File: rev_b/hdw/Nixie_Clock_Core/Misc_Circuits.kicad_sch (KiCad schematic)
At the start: 20 parts, among them U2401 LTC6900, U2402 74LVC1G08

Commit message: lots of rev B control board schematic progress
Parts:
- removed D?: MBR0580, Diode_SMD:D_SOD-123, symbol Diode:MBR0580
- removed U2402: 74LVC1G08, Package_TO_SOT_SMD:SOT-353_SC-70-5, symbol Custom_Library:74LVC1G08_Power
- added D?: SMD1200PL, Diodes_SMD:D_SOD-123F, symbol Nixie-Clock-rescue:D_Schottky
- added U?: 74LVC1G97, Package_TO_SOT_SMD:SOT-363_SC-70-6, symbol Custom Library:74LVC1G97_Power_AND
- renumbered BZ2401 to BZ?, R2406 to R?, U2401 to U?
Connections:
- net +3.3V: now also D?.1 (K), U?.5 (VCC)
- net Buzzer_Enable: now also U?.3
- net GND: now also U?.1 (GND), U?.2 (GND)
- net at BZ?.2 (+), Q?.3 (D): now also D?.2 (A)
- net at R?.2, U?.5 (OUT): now also U?.6
- net at R?.2: now also U?.4

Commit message: more rev b sch progress
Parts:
- removed J?: DAC SPI, Pin_Headers:Pin_Header_Straight_1x03_Pitch2.54mm, symbol Connector_Generic:Conn_01x03
- added R? (x2): 10k, Resistors_SMD:R_0603, symbol Custom_Library:R_Custom
- added R? (x2): 10, Resistors_SMD:R_0603, symbol Custom_Library:R_Custom
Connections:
- net +3.3V: now also R?.1, R?.1
- net GND: now also R?.2, R?.2
- new net ETC_Hardstrap: R?.1, R?.2
- new net RTC_Hardstrap: R?.1, R?.2
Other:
- moved on the sheet: BZ?, C?, D?, J?, Q?, R?, U?

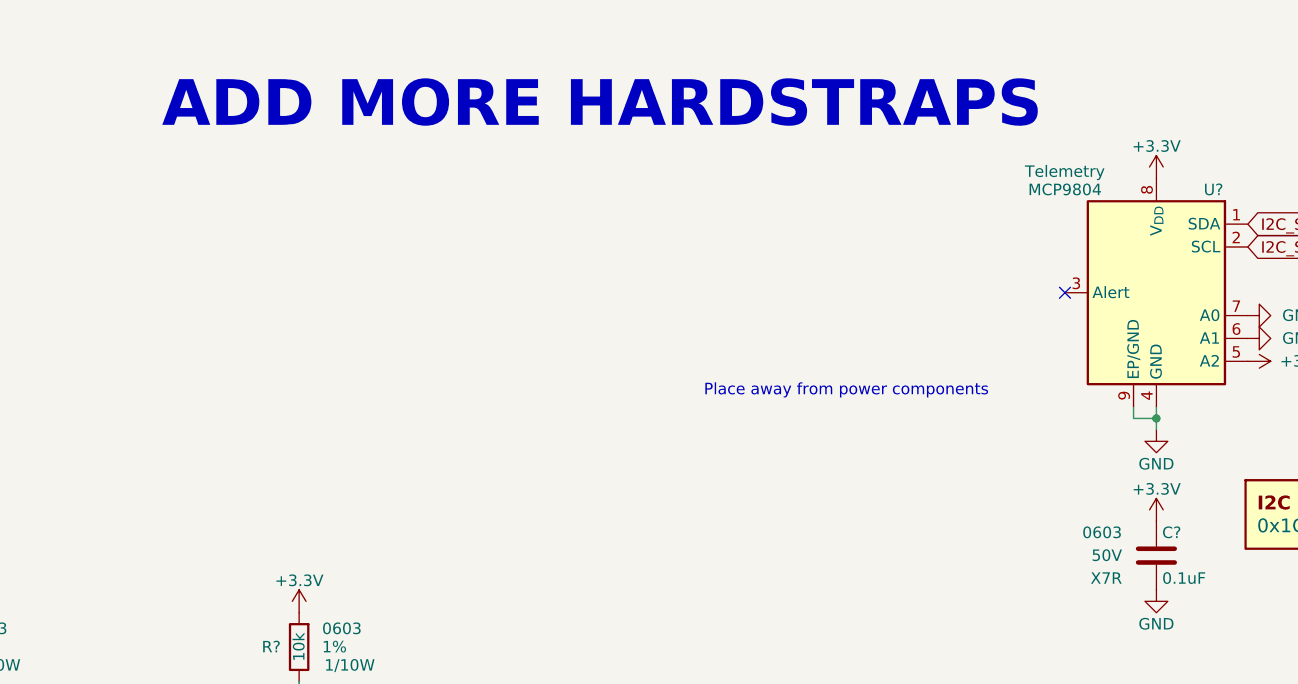
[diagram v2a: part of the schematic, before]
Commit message: more schematic progress, assigning signals to MCU"
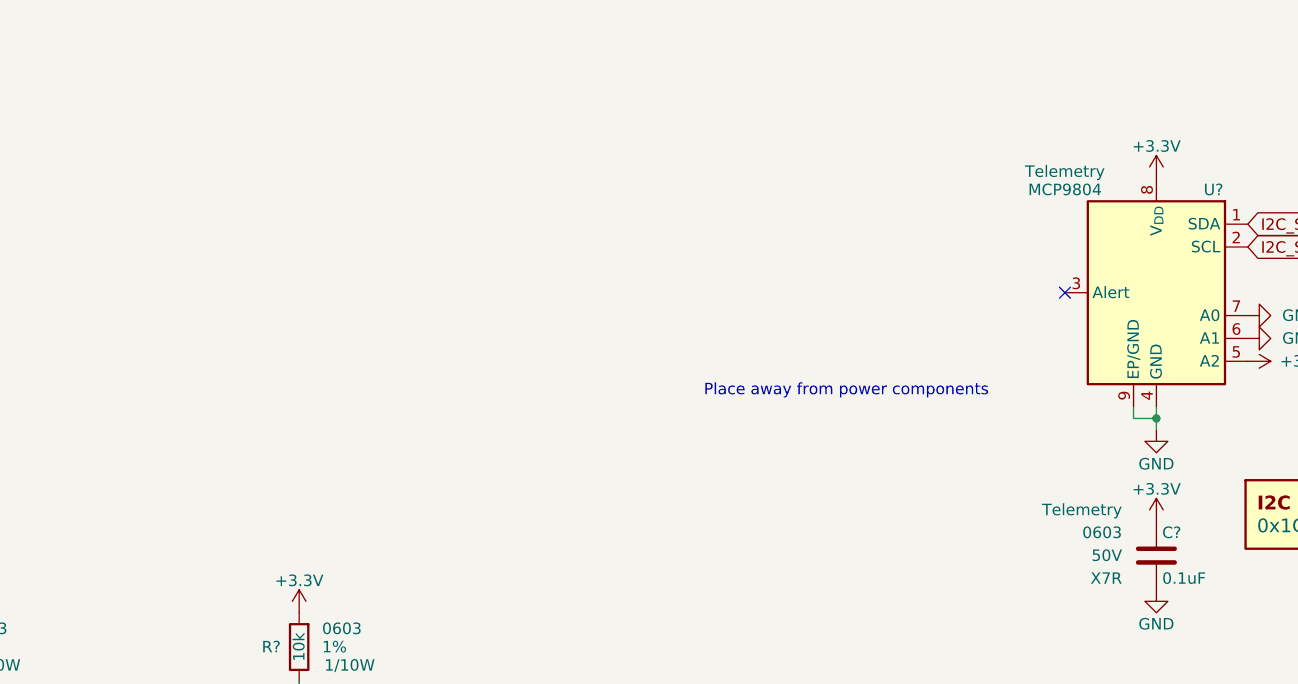
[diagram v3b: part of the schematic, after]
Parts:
- C?: Configuration (none) -> Telemetry
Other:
- note removed: "ADD MORE HARDSTRAPS"
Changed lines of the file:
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@@
     (stroke (width 0) (type default))
-  )
-  (text "ADD MORE HARDSTRAPS" (at 96.52 31.75 0)
-    (effects (font (face "Courier New") (size 5.08 5.08) (thickness 0.254) bold (color 255 37 56 1)) (justify left bottom))
   )
   (text "Fosc ~ 2kHz" (at 53.213 158.115 0)
@@
       (effects (font (size 1.27 1.27)) hide)
     )
-    (pin "1")
+    (property "Configuration" "Telemetry" (at 203.2 73.66 0)
+      (effects (font (size 1.27 1.27)) (justify right))
+    )
+    (pin "1")

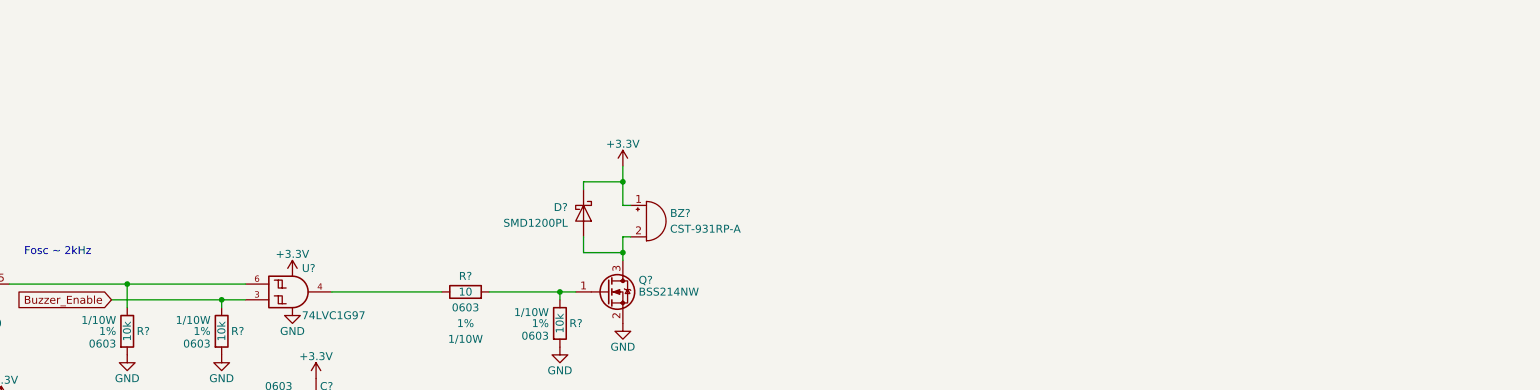
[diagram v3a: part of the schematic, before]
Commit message: updated footprints, ran some DRC
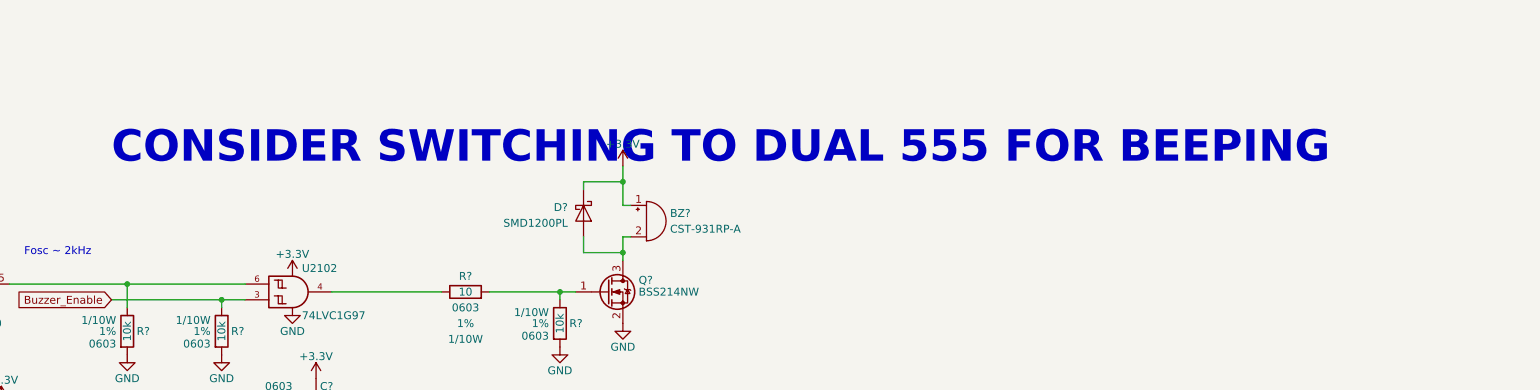
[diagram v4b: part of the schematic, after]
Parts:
- C? (x3): Digi-Key PN 399-7845-1-ND -> (none)
- D?: Footprint Display SOD-123F -> (none); display_footprint (none) -> SOD-123F
- J? (x2): footprint Pin_Headers:Pin_Header_Straight_1x03_Pitch2.54mm -> Connector_PinHeader_2.54mm:PinHeader_1x03_P2.54mm_Vertical
- Q?: footprint TO_SOT_Packages_SMD:SOT-323_SC-70 -> Package_TO_SOT_SMD:SOT-323_SC-70
- R? (x7): Digi-Key PN YAG2321CT-ND -> (none)
- R?: Digi-Key PN RMCF0603FT1M07CT-ND -> (none)
- gave numbers to parts that had none: 1
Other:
- note added: "CONSIDER SWITCHING TO DUAL 555 FOR BEEPING"

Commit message: hid all passive refdes on core PCB
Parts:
- C? (x3): Digi-Key PN (none) -> 1276-1935-1-ND
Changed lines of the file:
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@@
       (effects (font (size 1.27 1.27)) (justify right))
     )
-    (property "Digi-Key PN" "" (at 1.016 356.362 0)
+    (property "Digi-Key PN" "1276-1935-1-ND" (at 1.016 356.362 0)
       (effects (font (size 1.27 1.27)) hide)
     )
@@
       (effects (font (size 1.27 1.27)) (justify right))
     )
-    (property "Digi-Key PN" "" (at 107.696 253.492 0)
+    (property "Digi-Key PN" "1276-1935-1-ND" (at 107.696 253.492 0)
       (effects (font (size 1.27 1.27)) hide)
     )
@@
       (effects (font (size 1.27 1.27)) (justify right))
     )
-    (property "Digi-Key PN" "" (at -49.784 360.172 0)
+    (property "Digi-Key PN" "1276-1935-1-ND" (at -49.784 360.172 0)
       (effects (font (size 1.27 1.27)) hide)
     )

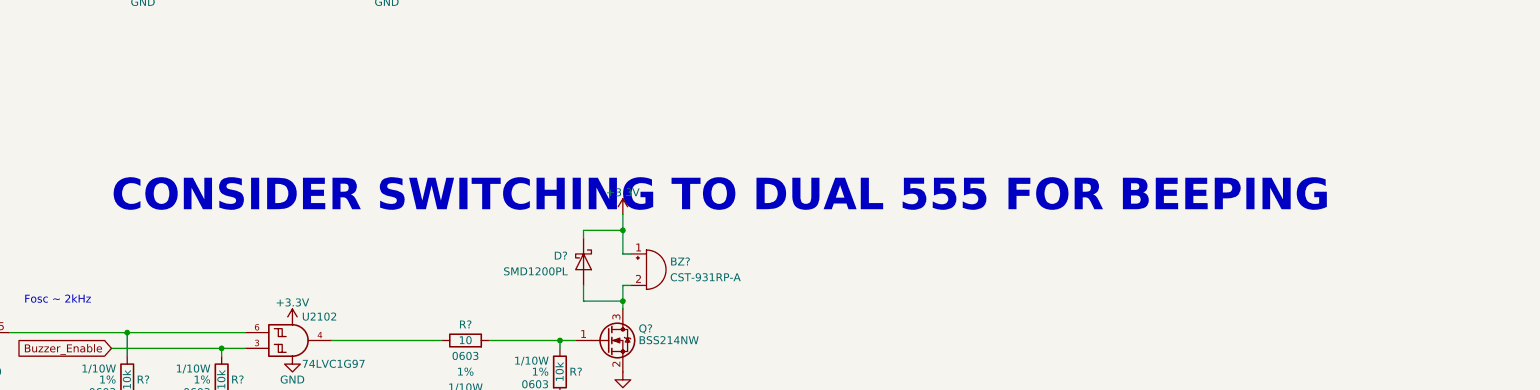
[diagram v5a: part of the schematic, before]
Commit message: added BOM
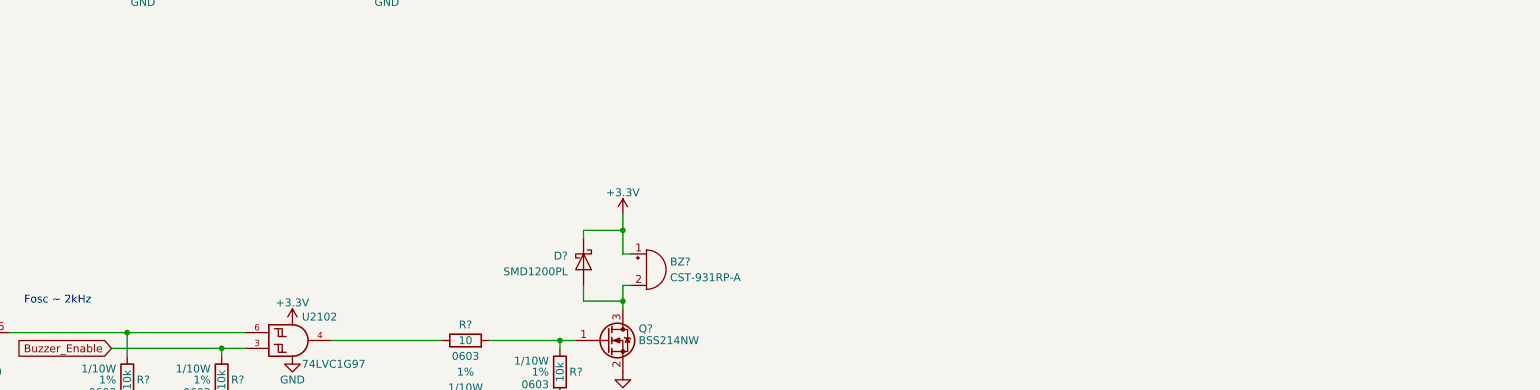
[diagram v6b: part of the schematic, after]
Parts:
- D?: Digi-Key PN (none) -> SMD1200PL-TPMSCT-ND
- R? (x4): Digi-Key PN (none) -> 541-10.0HCT-ND
- R? (x6): Digi-Key PN (none) -> 541-10.0KHCT-ND
- R?: Digi-Key PN (none) -> 541-1.07MHCT-ND
- U2102: Digi-Key PN (none) -> 296-15582-1-ND
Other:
- note removed: "CONSIDER SWITCHING TO DUAL 555 FOR BEEPING"
- company: (none) -> Drew Maatman
- title: (none) -> Nixie Clock Redux Core Board
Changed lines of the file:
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@@
 (kicad_sch (version 20230121) (generator eeschema)
   (paper "A4")
+  (title_block
+    (title "Nixie Clock Redux Core Board")
+    (date "2023-07-30")
+    (rev "B")
+    (company "Drew Maatman")
+  )
   (junction (at 111.76 95.25) (diameter 0) (color 0 0 0 0)
   )
@@
     (effects (font (size 1.27 1.27)) (justify left bottom))
   )
-  (text "CONSIDER SWITCHING TO DUAL 555 FOR BEEPING" (at 67.31 143.51 0)
-    (effects (font (face "Courier New") (size 5.08 5.08) (thickness 0.254) bold (color 255 37 56 1)) (justify left bottom))
-  )
-  (global_label "USB_UART_RX" (shape passive) (at 36.83 44.45 180)
+  (global_label "USB_UART_RX" (shape passive) (at 36.83 44.45 180) (fields_autoplaced)
     (effects (font (size 1.27 1.27)) (justify right))
-    (property "Intersheetrefs" "${INTERSHEET_REFS}" (at 36.83 44.45 0)
-      (effects (font (size 1.27 1.27)) hide)
-    )
-  )
-  (global_label "USB_UART_TX" (shape passive) (at 36.83 41.91 180)
+    (property "Intersheetrefs" "${INTERSHEET_REFS}" (at 22.1541 44.45 0)
+      (effects (font (size 1.27 1.27)) (justify right))
+    )
+  )
+  (global_label "USB_UART_TX" (shape passive) (at 36.83 41.91 180) (fields_autoplaced)
     (effects (font (size 1.27 1.27)) (justify right))
-    (property "Intersheetrefs" "${INTERSHEET_REFS}" (at 36.83 41.91 0)
-      (effects (font (size 1.27 1.27)) hide)
-    )
-  )
-  (global_label "ETC_Hardstrap" (shape passive) (at 74.93 95.25 0)
+    (property "Intersheetrefs" "${INTERSHEET_REFS}" (at 22.4565 41.91 0)
+      (effects (font (size 1.27 1.27)) (justify right))
+    )
+  )
+  (global_label "ETC_Hardstrap" (shape passive) (at 74.93 95.25 0) (fields_autoplaced)
     (effects (font (size 1.27 1.27)) (justify left))
-    (property "Intersheetrefs" "${INTERSHEET_REFS}" (at 74.93 95.25 0)
-      (effects (font (size 1.27 1.27)) hide)
-    )
-  )
-  (global_label "I2C_SDA" (shape bidirectional) (at 217.17 41.91 0)
+    (property "Intersheetrefs" "${INTERSHEET_REFS}" (at 90.3314 95.25 0)
+      (effects (font (size 1.27 1.27)) (justify left))
+    )
+  )
+  (global_label "I2C_SDA" (shape bidirectional) (at 217.17 41.91 0) (fields_autoplaced)
     (effects (font (size 1.27 1.27)) (justify left))
-    (property "Intersheetrefs" "${INTERSHEET_REFS}" (at 217.17 41.91 0)
-      (effects (font (size 1.27 1.27)) hide)
-    )
-  )
-  (global_label "RTC_Hardstrap" (shape passive) (at 114.3 95.25 0)
+    (property "Intersheetrefs" "${INTERSHEET_REFS}" (at 228.8071 41.91 0)
+      (effects (font (size 1.27 1.27)) (justify left))
+    )
+  )
+  (global_label "RTC_Hardstrap" (shape passive) (at 114.3 95.25 0) (fields_autoplaced)
     (effects (font (size 1.27 1.27)) (justify left))
-    (property "Intersheetrefs" "${INTERSHEET_REFS}" (at 114.3 95.25 0)
-      (effects (font (size 1.27 1.27)) hide)
-    )
-  )
-  (global_label "Buzzer_Enable" (shape input) (at 67.31 165.1 180)
+    (property "Intersheetrefs" "${INTERSHEET_REFS}" (at 129.8224 95.25 0)
+      (effects (font (size 1.27 1.27)) (justify left))
+    )
+  )
+  (global_label "Buzzer_Enable" (shape input) (at 67.31 165.1 180) (fields_autoplaced)
     (effects (font (size 1.27 1.27)) (justify right))
-    (property "Intersheetrefs" "${INTERSHEET_REFS}" (at 67.31 165.1 0)
-      (effects (font (size 1.27 1.27)) hide)
-    )
-  )
-  (global_label "I2C_SCL" (shape passive) (at 36.83 22.86 180)
+    (property "Intersheetrefs" "${INTERSHEET_REFS}" (at 50.7368 165.1 0)
+      (effects (font (size 1.27 1.27)) (justify right))
+    )
+  )
+  (global_label "I2C_SCL" (shape passive) (at 36.83 22.86 180) (fields_autoplaced)
     (effects (font (size 1.27 1.27)) (justify right))
-    (property "Intersheetrefs" "${INTERSHEET_REFS}" (at 36.83 22.86 0)
-      (effects (font (size 1.27 1.27)) hide)
-    )
-  )
-  (global_label "Telemetry_Hardstrap" (shape passive) (at 36.83 95.25 0)
+    (property "Intersheetrefs" "${INTERSHEET_REFS}" (at 27.476 22.86 0)
+      (effects (font (size 1.27 1.27)) (justify right))
+    )
+  )
+  (global_label "Telemetry_Hardstrap" (shape passive) (at 36.83 95.25 0) (fields_autoplaced)
     (effects (font (size 1.27 1.27)) (justify left))
-    (property "Intersheetrefs" "${INTERSHEET_REFS}" (at 36.83 95.25 0)
-      (effects (font (size 1.27 1.27)) hide)
-    )
-  )
-  (global_label "I2C_SDA" (shape passive) (at 36.83 25.4 180)
+    (property "Intersheetrefs" "${INTERSHEET_REFS}" (at 57.9162 95.25 0)
+      (effects (font (size 1.27 1.27)) (justify left))
+    )
+  )
+  (global_label "I2C_SDA" (shape passive) (at 36.83 25.4 180) (fields_autoplaced)
     (effects (font (size 1.27 1.27)) (justify right))
-    (property "Intersheetrefs" "${INTERSHEET_REFS}" (at 36.83 25.4 0)
-      (effects (font (size 1.27 1.27)) hide)
-    )
-  )
-  (global_label "I2C_SCL" (shape input) (at 217.17 44.45 0)
+    (property "Intersheetrefs" "${INTERSHEET_REFS}" (at 27.4155 25.4 0)
+      (effects (font (size 1.27 1.27)) (justify right))
+    )
+  )
+  (global_label "I2C_SCL" (shape input) (at 217.17 44.45 0) (fields_autoplaced)
     (effects (font (size 1.27 1.27)) (justify left))
-    (property "Intersheetrefs" "${INTERSHEET_REFS}" (at 217.17 44.45 0)
-      (effects (font (size 1.27 1.27)) hide)
+    (property "Intersheetrefs" "${INTERSHEET_REFS}" (at 227.6353 44.45 0)
+      (effects (font (size 1.27 1.27)) (justify left))
     )
   )
@@
       (effects (font (size 1.27 1.27)))
     )
+    (property "Digi-Key PN" "541-10.0HCT-ND" (at 34.29 101.6 0)
+      (effects (font (size 1.27 1.27)) hide)
+    )
     (pin "1")
     (pin "2")
@@
       (effects (font (size 1.27 1.27)) (justify left))
     )
-    (property "Digi-Key PN" "" (at 188.976 28.194 0)
+    (property "Digi-Key PN" "541-10.0KHCT-ND" (at 188.976 28.194 0)
       (effects (font (size 1.27 1.27)) hide)
     )
@@
       (effects (font (size 1.27 1.27)) (justify left))
     )
-    (property "Digi-Key PN" "" (at 80.01 78.74 0)
+    (property "Digi-Key PN" "541-10.0KHCT-ND" (at 80.01 78.74 0)
       (effects (font (size 1.524 1.524)) hide)
     )
@@
       (effects (font (size 1.27 1.27)) (justify left))
     )
-    (property "Digi-Key PN" "" (at 41.91 78.74 0)
+    (property "Digi-Key PN" "541-10.0KHCT-ND" (at 41.91 78.74 0)
       (effects (font (size 1.524 1.524)) hide)
     )
@@
       (effects (font (size 1.27 1.27)) (justify left))
     )
-    (property "Digi-Key PN" "" (at 27.94 153.67 0)
+    (property "Digi-Key PN" "541-1.07MHCT-ND" (at 27.94 153.67 0)
       (effects (font (size 1.27 1.27)) hide)
     )
@@
       (effects (font (size 1.27 1.27)) (justify left))
     )
-    (property "Digi-Key PN" "" (at 119.38 78.74 0)
+    (property "Digi-Key PN" "541-10.0KHCT-ND" (at 119.38 78.74 0)
       (effects (font (size 1.524 1.524)) hide)
     )
@@
       (effects (font (size 1.27 1.27)) hide)
     )
-    (property "Digi-Key PN" "" (at 134.62 171.45 0)
+    (property "Digi-Key PN" "541-10.0HCT-ND" (at 134.62 171.45 0)
       (effects (font (size 1.524 1.524)) hide)
     )
@@
     )
     (property "Datasheet" "http://www.ti.com/lit/ds/symlink/sn74lvc1g97.pdf" (at 97.79 163.83 0)
+      (effects (font (size 1.27 1.27)) hide)
+    )
+    (property "Digi-Key PN" "296-15582-1-ND" (at 96.52 163.83 0)
       (effects (font (size 1.27 1.27)) hide)
     )
@@
     (property "Configuration" "BACKUP_RTC" (at 114.3 105.41 0)
       (effects (font (size 1.27 1.27)) (justify left))
+    )
+    (property "Digi-Key PN" "541-10.0HCT-ND" (at 111.76 101.6 0)
+      (effects (font (size 1.27 1.27)) hide)
     )
     (pin "1")
@@
       (effects (font (size 1.27 1.27)) (justify left))
     )
+    (property "Digi-Key PN" "541-10.0HCT-ND" (at 72.39 101.6 0)
+      (effects (font (size 1.27 1.27)) hide)
+    )
     (pin "1")
     (pin "2")
@@
       (effects (font (size 1.27 1.27)) (justify left))
     )
-    (property "Digi-Key PN" "" (at 173.736 28.194 0)
+    (property "Digi-Key PN" "541-10.0KHCT-ND" (at 173.736 28.194 0)
       (effects (font (size 1.27 1.27)) hide)
     )
@@
       (effects (font (size 1.27 1.27)) (justify left))
     )
-    (property "Digi-Key PN" "" (at 243.586 26.924 0)
+    (property "Digi-Key PN" "541-10.0KHCT-ND" (at 243.586 26.924 0)
       (effects (font (size 1.27 1.27)) hide)
     )
@@
       (effects (font (size 1.27 1.27)) hide)
     )
+    (property "Digi-Key PN" "SMD1200PL-TPMSCT-ND" (at 143.51 151.13 0)
+      (effects (font (size 1.27 1.27)) hide)
+    )
